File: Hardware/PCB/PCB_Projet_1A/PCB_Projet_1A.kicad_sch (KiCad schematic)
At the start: 23 parts, among them J1 Conn_01x03, J2 Conn_01x04, J3 Conn_01x03, J4 Conn_01x04, J5 Conn_01x04, J6 Conn_ST_STDC14, J7 Conn_01x04, J8 Conn_01x02, J9 Conn_01x02, U1 HC-05

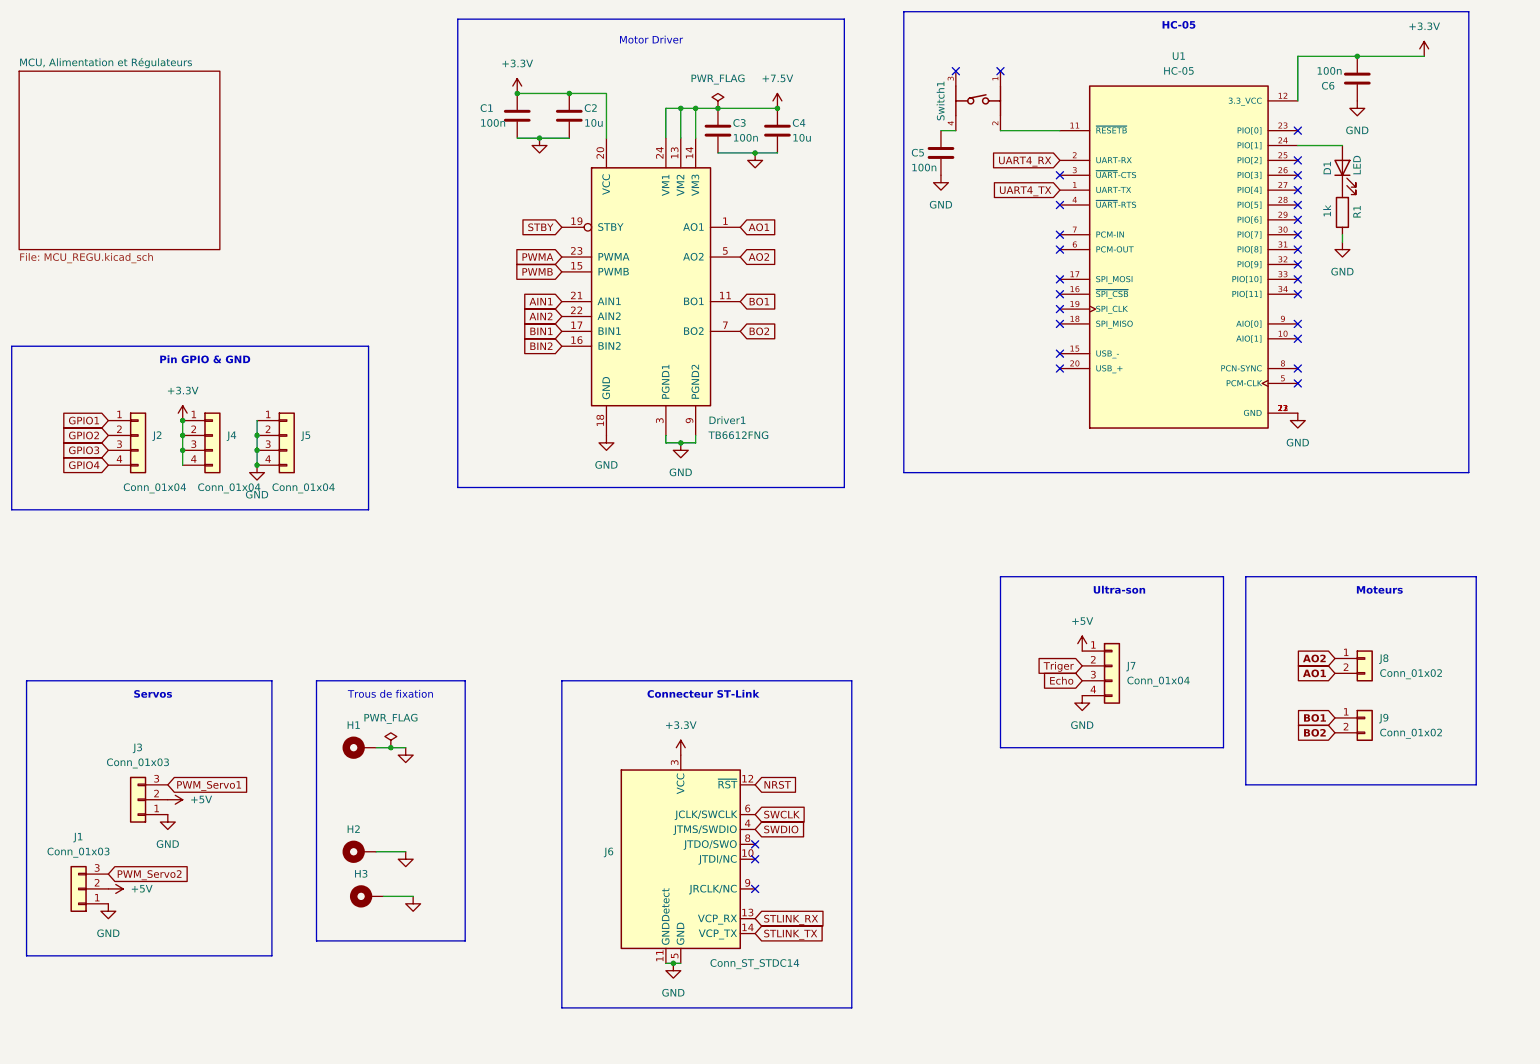
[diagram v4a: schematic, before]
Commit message: Modification du PCB: changement du HC05 SMD en pinheader adapté au module
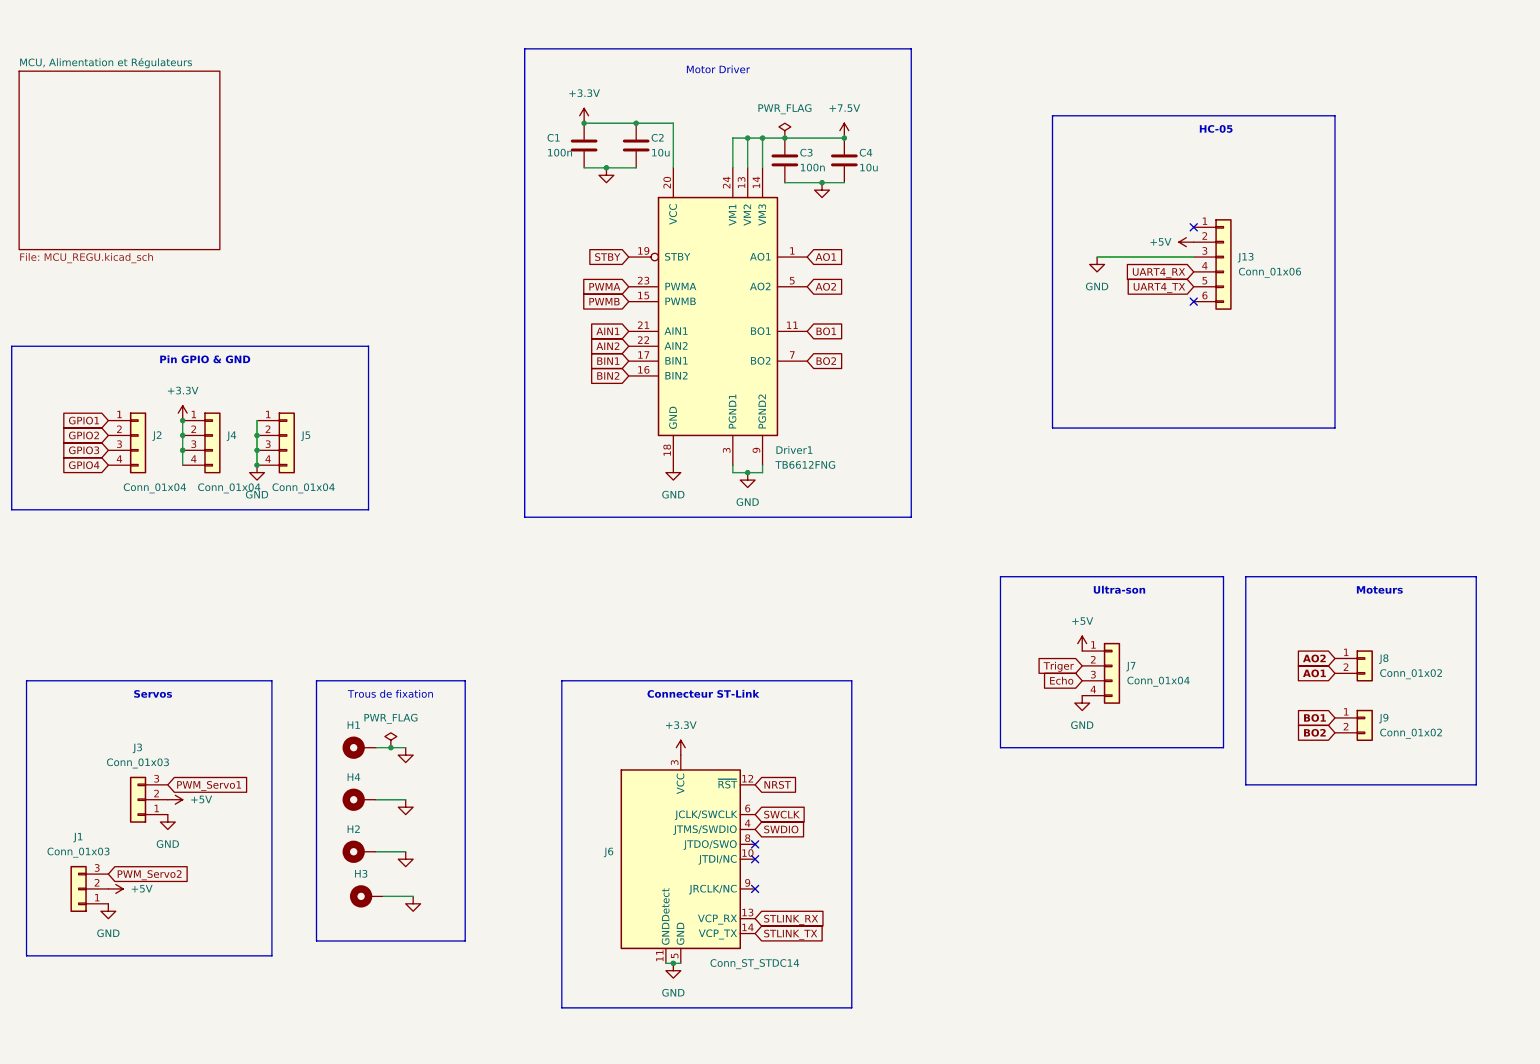
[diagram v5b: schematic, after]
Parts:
- removed C5, C6: 100n, Capacitor_SMD:C_0402_1005Metric, symbol Device:C
- removed D1: LED, LED_SMD:LED_0603_1608Metric_Pad1.05x0.95mm_HandSolder, symbol Device:LED
- removed R1: 1k, Resistor_SMD:R_0603_1608Metric_Pad0.98x0.95mm_HandSolder, symbol Device:R
- removed Switch1: 430471025826, boutonSMD_wurth430471025826:430471025826, symbol boutonSMD_wurth430471025826:430471025826
- removed U1: HC-05, HC-05:XCVR_HC-05, symbol HC-05:HC-05
- added H4: MountingHole_Pad, MountingHole:MountingHole_2.7mm_M2.5_Pad, symbol Mechanical:MountingHole_Pad
- added J13: Conn_01x06, Connector_PinHeader_2.54mm:PinHeader_1x06_P2.54mm_Vertical, symbol Connector_Generic:Conn_01x06
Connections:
- net +5V: now also J13.2 (Pin_2)
- net GND: now also H4.1, J13.3 (Pin_3)
- net UART4_RX: now also J13.4 (Pin_4)
- net UART4_TX: now also J13.5 (Pin_5)
- no-connect marks 30 -> 5
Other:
- moved on the sheet: C1, C2, C3, C4, Driver1

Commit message: modif pcb
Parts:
- removed J2, J4, J5: Conn_01x04, Connector_PinHeader_2.54mm:PinHeader_1x04_P2.54mm_Vertical, symbol Connector_Generic:Conn_01x04
- added J14, J15, J16: Conn_01x03, Connector_PinHeader_2.54mm:PinHeader_1x03_P2.54mm_Vertical, symbol Connector_Generic:Conn_01x03
- added J2: Conn_01x02, Connector_PinHeader_2.54mm:PinHeader_1x02_P2.54mm_Horizontal, symbol Connector_Generic:Conn_01x02
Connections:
- net +3.3V: now also J16.1 (Pin_1), J16.2 (Pin_2), J16.3 (Pin_3)
- net GND: now also J15.1 (Pin_1), J15.2 (Pin_2), J15.3 (Pin_3)
- net GPIO1: now also J14.1 (Pin_1)
- net GPIO2: now also J14.2 (Pin_2)
- net GPIO3: now also J14.3 (Pin_3)
- new net UART3_RX: J2.2 (Pin_2)
- new net UART3_TX: J2.1 (Pin_1)
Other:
- note added: "communication RASPBERRY"
